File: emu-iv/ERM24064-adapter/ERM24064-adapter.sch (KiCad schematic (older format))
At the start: 5 parts, among them J1 ERM24064-1-display, J2 ERM24064-1-mainboard, J3 Backlight_Connector_Mainboard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

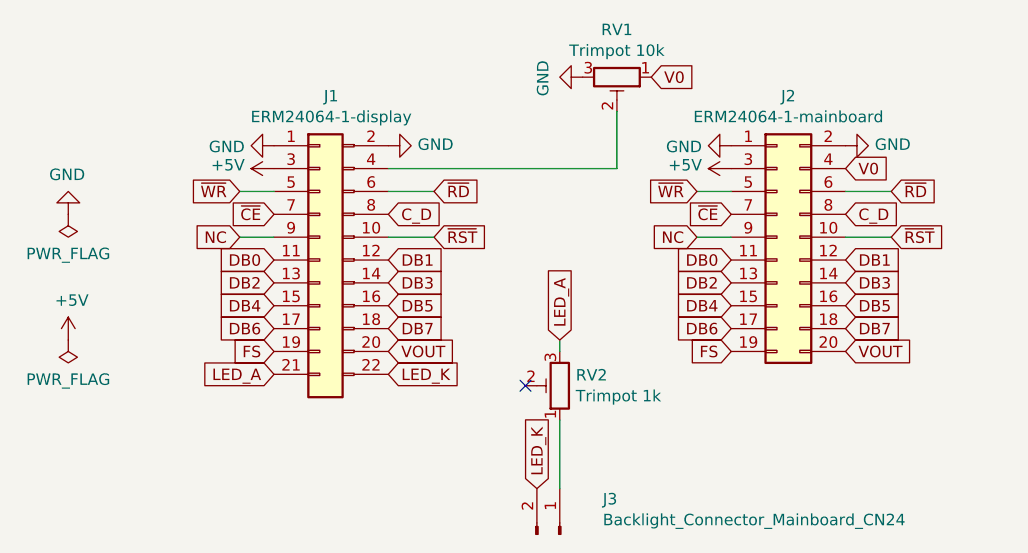
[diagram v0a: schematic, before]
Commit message: correction wrt. to the current limiting resistor for the backlight led.
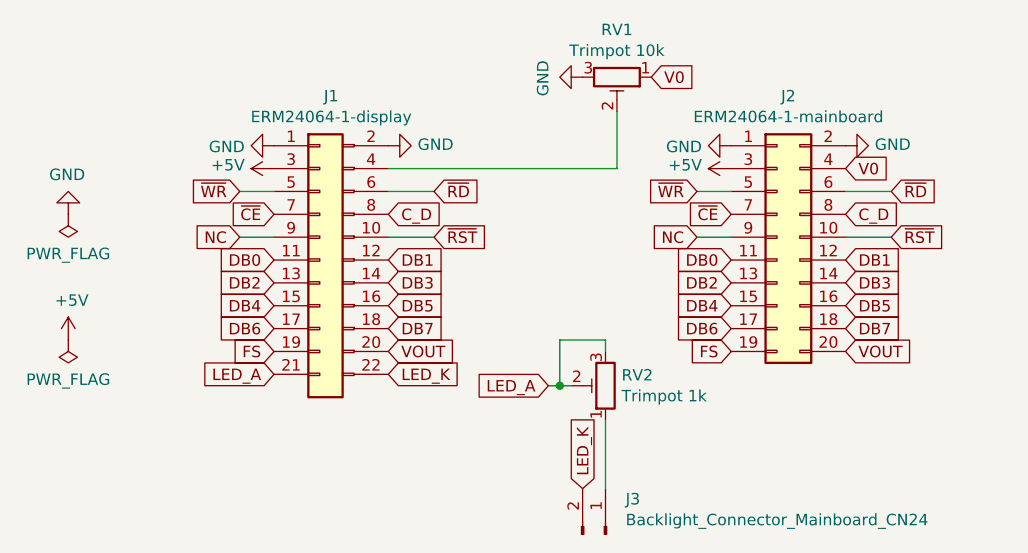
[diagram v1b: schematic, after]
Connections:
- net LED_A: now also RV2.2
- no-connect marks 1 -> 0
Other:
- moved on the sheet: RV2
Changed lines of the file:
@@
 L Device:R_POT_TRIM RV2
 U 1 1 60F41176
-P 2900 3250
-F 0 "RV2" H 2830 3204 50  0000 R CNN
-F 1 "Trimpot 1k" H 2830 3295 50  0000 R CNN
-F 2 "Potentiometer_THT:Potentiometer_ACP_CA9-V10_Vertical" H 2900 3250 50  0001 C CNN
-F 3 "~" H 2900 3250 50  0001 C CNN
-	1    2900 3250
+P 3100 3250
+F 0 "RV2" H 3030 3204 50  0000 R CNN
+F 1 "Trimpot 1k" H 3030 3295 50  0000 R CNN
+F 2 "Potentiometer_THT:Potentiometer_ACP_CA9-V10_Vertical" H 3100 3250 50  0001 C CNN
+F 3 "~" H 3100 3250 50  0001 C CNN
+	1    3100 3250
 	-1   0    0    1
 $EndComp
-$Comp
-L ERM24064-adapter:Backlight_Connector_Mainboard_CN24 J3
-U 1 1 60F4B848
-P 2800 3900
-F 0 "J3" V 2954 3612 50  0000 R CNN
-F 1 "Backlight_Connector_Mainboard_CN24" V 2863 3612 50  0000 R CNN
-F 2 "Connector_Molex:Molex_KK-254_AE-6410-02A_1x02_P2.54mm_Vertical" H 2800 3900 50  0001 C CNN
-F 3 "~" H 2800 3900 50  0001 C CNN
-	1    2800 3900
-	0    -1   -1   0
-$EndComp
-NoConn ~ 2750 3250
-Text GLabel 2900 3050 1    50   Input ~ 0
+Text GLabel 2850 3250 0    50   Input ~ 0
 LED_A
-Text GLabel 2800 3700 1    50   Input ~ 0
+Text GLabel 3000 3700 1    50   Input ~ 0
 LED_K
 Wire Wire Line
-	2900 3700 2900 3400
+	3100 3700 3100 3400
 Wire Wire Line
-	2900 3100 2900 3050
+	3100 3100 3100 3050
 Text GLabel 1650 3200 0    50   Input ~ 0
 LED_A
 Text GLabel 2150 3200 2    50   Input ~ 0
 LED_K
+Wire Wire Line
+	2950 3250 2900 3250
+Wire Wire Line
+	3100 3050 2900 3050
+Wire Wire Line
+	2900 3050 2900 3250
+Connection ~ 2900 3250
+Wire Wire Line
+	2900 3250 2850 3250
+$Comp
+L ERM24064-adapter:Backlight_Connector_Mainboard_CN24 J3
+U 1 1 60F0E76F
+P 3000 3900
+F 0 "J3" V 3154 3712 50  0000 R CNN
+F 1 "Backlight_Connector_Mainboard_CN24" V 3063 3712 50  0000 R CNN
+F 2 "Connector_Molex:Molex_KK-254_AE-6410-02A_1x02_P2.54mm_Vertical" H 3000 3900 50  0001 C CNN
+F 3 "~" H 3000 3900 50  0001 C CNN
+	1    3000 3900
+	0    -1   -1   0
+$EndComp
 $EndSCHEMATC
